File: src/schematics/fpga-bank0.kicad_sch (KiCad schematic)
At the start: 7 parts

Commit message: Updates the root page
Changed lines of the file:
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@@
+		)
+	)
+	(hierarchical_label "SRAM_A[0..12]"
+		(shape input)
+		(at 40.64 54.61 180)
+		(fields_autoplaced yes)
+		(effects
+			(font
+				(size 1.27 1.27)
+			)
+			(justify right)
 		)
 	)
@@
 		)
 	)
-	(hierarchical_label "{SDRAM}"
+	(hierarchical_label "SRAM_DQ[0..15]"
 		(shape input)
-		(at 95.25 59.69 180)
+		(at 73.66 116.84 0)
 		(fields_autoplaced yes)
 		(effects
@@
 				(size 1.27 1.27)
 			)
+			(justify left)
+		)
+	)
+	(hierarchical_label "SRAM_BA[0..1]"
+		(shape input)
+		(at 41.91 90.17 180)
+		(fields_autoplaced yes)
+		(effects
+			(font
+				(size 1.27 1.27)
+			)
 			(justify right)
+		)
+	)
+	(hierarchical_label "SRAM_~{WE}"
+		(shape input)
+		(at 54.61 124.46 0)
+		(fields_autoplaced yes)
+		(effects
+			(font
+				(size 1.27 1.27)
+			)
+			(justify left)
+		)
+	)
+	(hierarchical_label "SRAM_CLK"
+		(shape input)
+		(at 60.96 104.14 180)
+		(fields_autoplaced yes)
+		(effects
+			(font
+				(size 1.27 1.27)
+			)
+			(justify right)
+		)
+	)
+	(hierarchical_label "SRAM_~{CS}"
+		(shape input)
+		(at 60.96 109.22 180)
+		(fields_autoplaced yes)
+		(effects
+			(font
+				(size 1.27 1.27)
+			)
+			(justify right)
+		)
+	)
+	(hierarchical_label "SRAM_~{RAS}"
+		(shape input)
+		(at 54.61 119.38 0)
+		(fields_autoplaced yes)
+		(effects
+			(font
+				(size 1.27 1.27)
+			)
+			(justify left)
+		)
+	)
+	(hierarchical_label "SRAM_~{CAS}"
+		(shape input)
+		(at 54.61 121.92 0)
+		(fields_autoplaced yes)
+		(effects
+			(font
+				(size 1.27 1.27)
+			)
+			(justify left)
+		)
+	)
+	(hierarchical_label "SRAM_DQML"
+		(shape input)
+		(at 54.61 114.3 0)
+		(fields_autoplaced yes)
+		(effects
+			(font
+				(size 1.27 1.27)
+			)
+			(justify left)
+		)
+	)
+	(hierarchical_label "SRAM_CKE"
+		(shape input)
+		(at 60.96 106.68 180)
+		(fields_autoplaced yes)
+		(effects
+			(font
+				(size 1.27 1.27)
+			)
+			(justify right)
+		)
+	)
+	(hierarchical_label "SRAM_DQMH"
+		(shape input)
+		(at 54.61 116.84 0)
+		(fields_autoplaced yes)
+		(effects
+			(font
+				(size 1.27 1.27)
+			)
+			(justify left)
 		)
 	)
@@
 		(instances
 			(project "ecap5-bsom"
-				(path "/c5fd18a3-9aa0-4151-b6e0-94da3d606686/9ec64d27-698a-408d-bb9c-7e381193a80d/a27a4945-d3aa-4752-b726-05ef96a067ff"
+				(path "/c5fd18a3-9aa0-4151-b6e0-94da3d606686/6e8ffa03-3d0b-48ef-9cef-06edc52c2bd8"
 					(reference "C48")
 					(unit 1)
@@
 		(instances
 			(project "ecap5-bsom"
-				(path "/c5fd18a3-9aa0-4151-b6e0-94da3d606686/9ec64d27-698a-408d-bb9c-7e381193a80d/a27a4945-d3aa-4752-b726-05ef96a067ff"
+				(path "/c5fd18a3-9aa0-4151-b6e0-94da3d606686/6e8ffa03-3d0b-48ef-9cef-06edc52c2bd8"
 					(reference "#PWR026")
 					(unit 1)
@@
 		(instances
 			(project "ecap5-bsom"
-				(path "/c5fd18a3-9aa0-4151-b6e0-94da3d606686/9ec64d27-698a-408d-bb9c-7e381193a80d/a27a4945-d3aa-4752-b726-05ef96a067ff"
+				(path "/c5fd18a3-9aa0-4151-b6e0-94da3d606686/6e8ffa03-3d0b-48ef-9cef-06edc52c2bd8"
 					(reference "C51")
 					(unit 1)
@@
 		(instances
 			(project "ecap5-bsom"
-				(path "/c5fd18a3-9aa0-4151-b6e0-94da3d606686/9ec64d27-698a-408d-bb9c-7e381193a80d/a27a4945-d3aa-4752-b726-05ef96a067ff"
+				(path "/c5fd18a3-9aa0-4151-b6e0-94da3d606686/6e8ffa03-3d0b-48ef-9cef-06edc52c2bd8"
 					(reference "#PWR029")
 					(unit 1)
@@
 		(instances
 			(project "ecap5-bsom"
-				(path "/c5fd18a3-9aa0-4151-b6e0-94da3d606686/9ec64d27-698a-408d-bb9c-7e381193a80d/a27a4945-d3aa-4752-b726-05ef96a067ff"
+				(path "/c5fd18a3-9aa0-4151-b6e0-94da3d606686/6e8ffa03-3d0b-48ef-9cef-06edc52c2bd8"
 					(reference "#PWR025")
 					(unit 1)
@@
 		(instances
 			(project "ecap5-bsom"
-				(path "/c5fd18a3-9aa0-4151-b6e0-94da3d606686/9ec64d27-698a-408d-bb9c-7e381193a80d/a27a4945-d3aa-4752-b726-05ef96a067ff"
+				(path "/c5fd18a3-9aa0-4151-b6e0-94da3d606686/6e8ffa03-3d0b-48ef-9cef-06edc52c2bd8"
 					(reference "#PWR028")
 					(unit 1)
@@
 		(instances
 			(project "ecap5-bsom"
-				(path "/c5fd18a3-9aa0-4151-b6e0-94da3d606686/9ec64d27-698a-408d-bb9c-7e381193a80d/a27a4945-d3aa-4752-b726-05ef96a067ff"
+				(path "/c5fd18a3-9aa0-4151-b6e0-94da3d606686/6e8ffa03-3d0b-48ef-9cef-06edc52c2bd8"
 					(reference "C52")
 					(unit 1)
@@
 		(instances
 			(project "ecap5-bsom"
-				(path "/c5fd18a3-9aa0-4151-b6e0-94da3d606686/9ec64d27-698a-408d-bb9c-7e381193a80d/a27a4945-d3aa-4752-b726-05ef96a067ff"
+				(path "/c5fd18a3-9aa0-4151-b6e0-94da3d606686/6e8ffa03-3d0b-48ef-9cef-06edc52c2bd8"
 					(reference "U6")
 					(unit 2)
@@
 		(instances
 			(project "ecap5-bsom"
-				(path "/c5fd18a3-9aa0-4151-b6e0-94da3d606686/9ec64d27-698a-408d-bb9c-7e381193a80d/a27a4945-d3aa-4752-b726-05ef96a067ff"
+				(path "/c5fd18a3-9aa0-4151-b6e0-94da3d606686/6e8ffa03-3d0b-48ef-9cef-06edc52c2bd8"
 					(reference "C50")
 					(unit 1)
@@
 		(instances
 			(project "ecap5-bsom"
-				(path "/c5fd18a3-9aa0-4151-b6e0-94da3d606686/9ec64d27-698a-408d-bb9c-7e381193a80d/a27a4945-d3aa-4752-b726-05ef96a067ff"
+				(path "/c5fd18a3-9aa0-4151-b6e0-94da3d606686/6e8ffa03-3d0b-48ef-9cef-06edc52c2bd8"
 					(reference "#PWR030")
 					(unit 1)
@@
 		(instances
 			(project "ecap5-bsom"
-				(path "/c5fd18a3-9aa0-4151-b6e0-94da3d606686/9ec64d27-698a-408d-bb9c-7e381193a80d/a27a4945-d3aa-4752-b726-05ef96a067ff"
+				(path "/c5fd18a3-9aa0-4151-b6e0-94da3d606686/6e8ffa03-3d0b-48ef-9cef-06edc52c2bd8"
 					(reference "#PWR031")
 					(unit 1)
@@
 		(instances
 			(project "ecap5-bsom"
-				(path "/c5fd18a3-9aa0-4151-b6e0-94da3d606686/9ec64d27-698a-408d-bb9c-7e381193a80d/a27a4945-d3aa-4752-b726-05ef96a067ff"
+				(path "/c5fd18a3-9aa0-4151-b6e0-94da3d606686/6e8ffa03-3d0b-48ef-9cef-06edc52c2bd8"
 					(reference "C53")
 					(unit 1)
@@
 		(instances
 			(project "ecap5-bsom"
-				(path "/c5fd18a3-9aa0-4151-b6e0-94da3d606686/9ec64d27-698a-408d-bb9c-7e381193a80d/a27a4945-d3aa-4752-b726-05ef96a067ff"
+				(path "/c5fd18a3-9aa0-4151-b6e0-94da3d606686/6e8ffa03-3d0b-48ef-9cef-06edc52c2bd8"
 					(reference "C49")
 					(unit 1)
@@
 		(instances
 			(project "ecap5-bsom"
-				(path "/c5fd18a3-9aa0-4151-b6e0-94da3d606686/9ec64d27-698a-408d-bb9c-7e381193a80d/a27a4945-d3aa-4752-b726-05ef96a067ff"
+				(path "/c5fd18a3-9aa0-4151-b6e0-94da3d606686/6e8ffa03-3d0b-48ef-9cef-06edc52c2bd8"
 					(reference "#PWR027")
 					(unit 1)

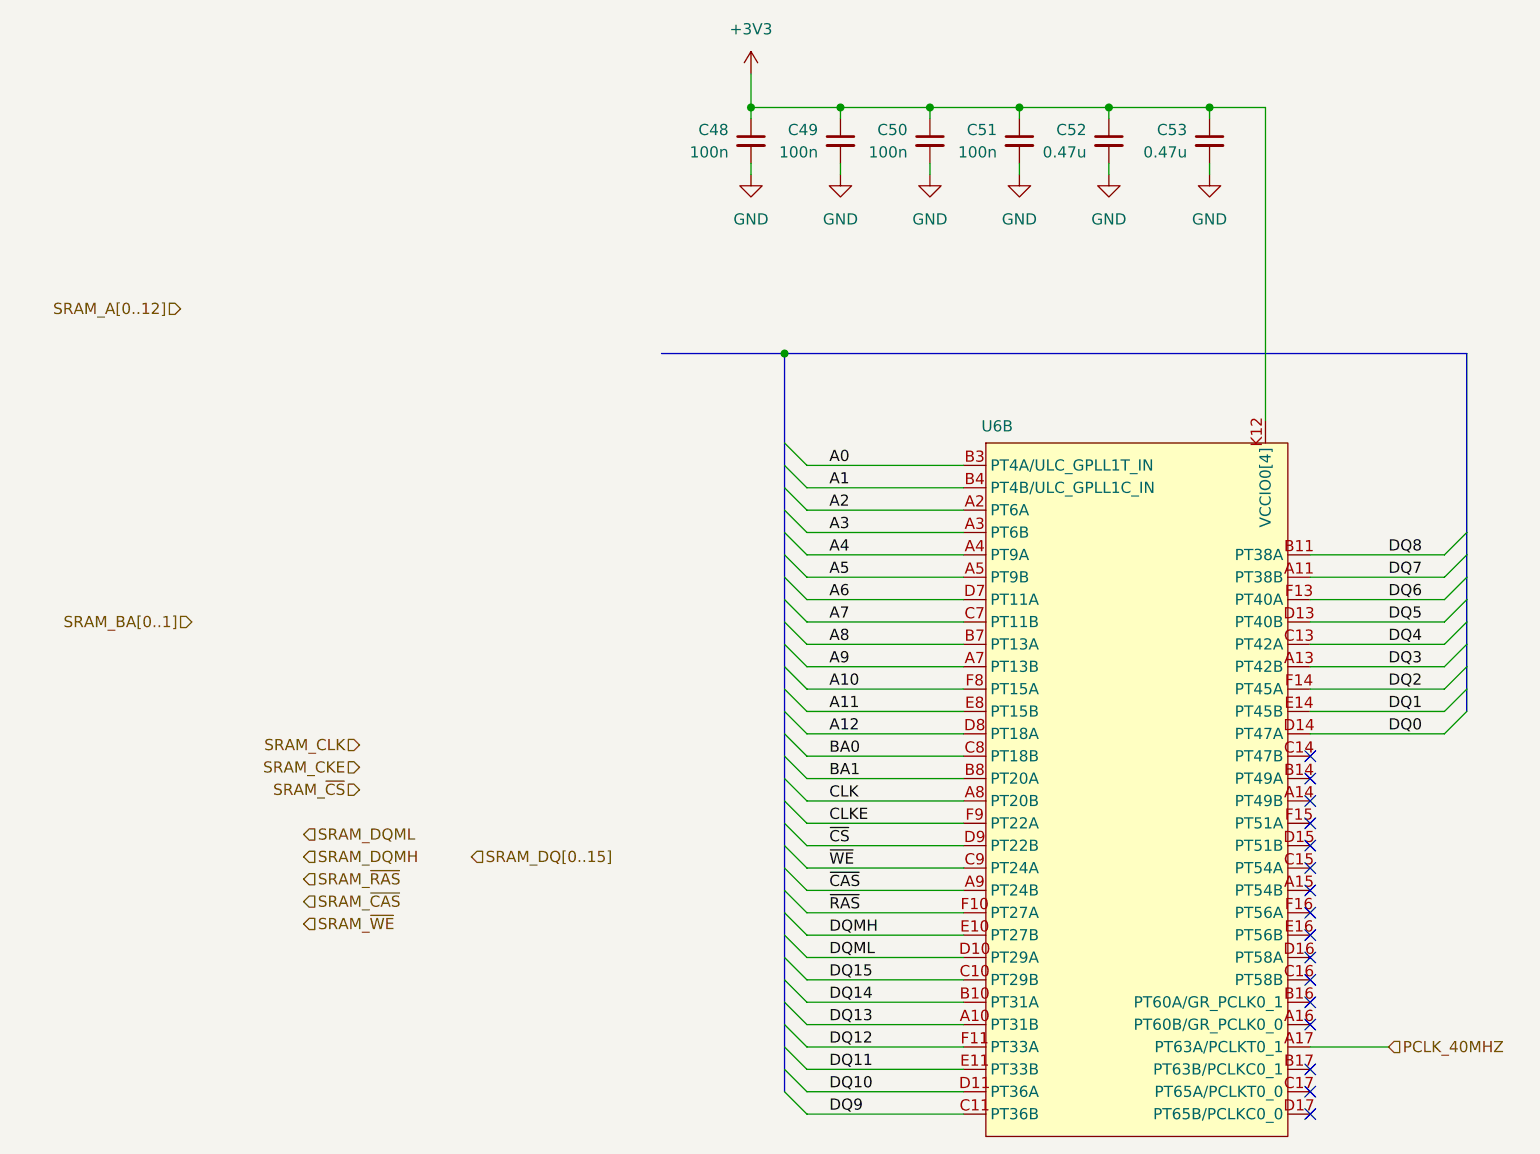
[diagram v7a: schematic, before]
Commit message: Adds a revision history table
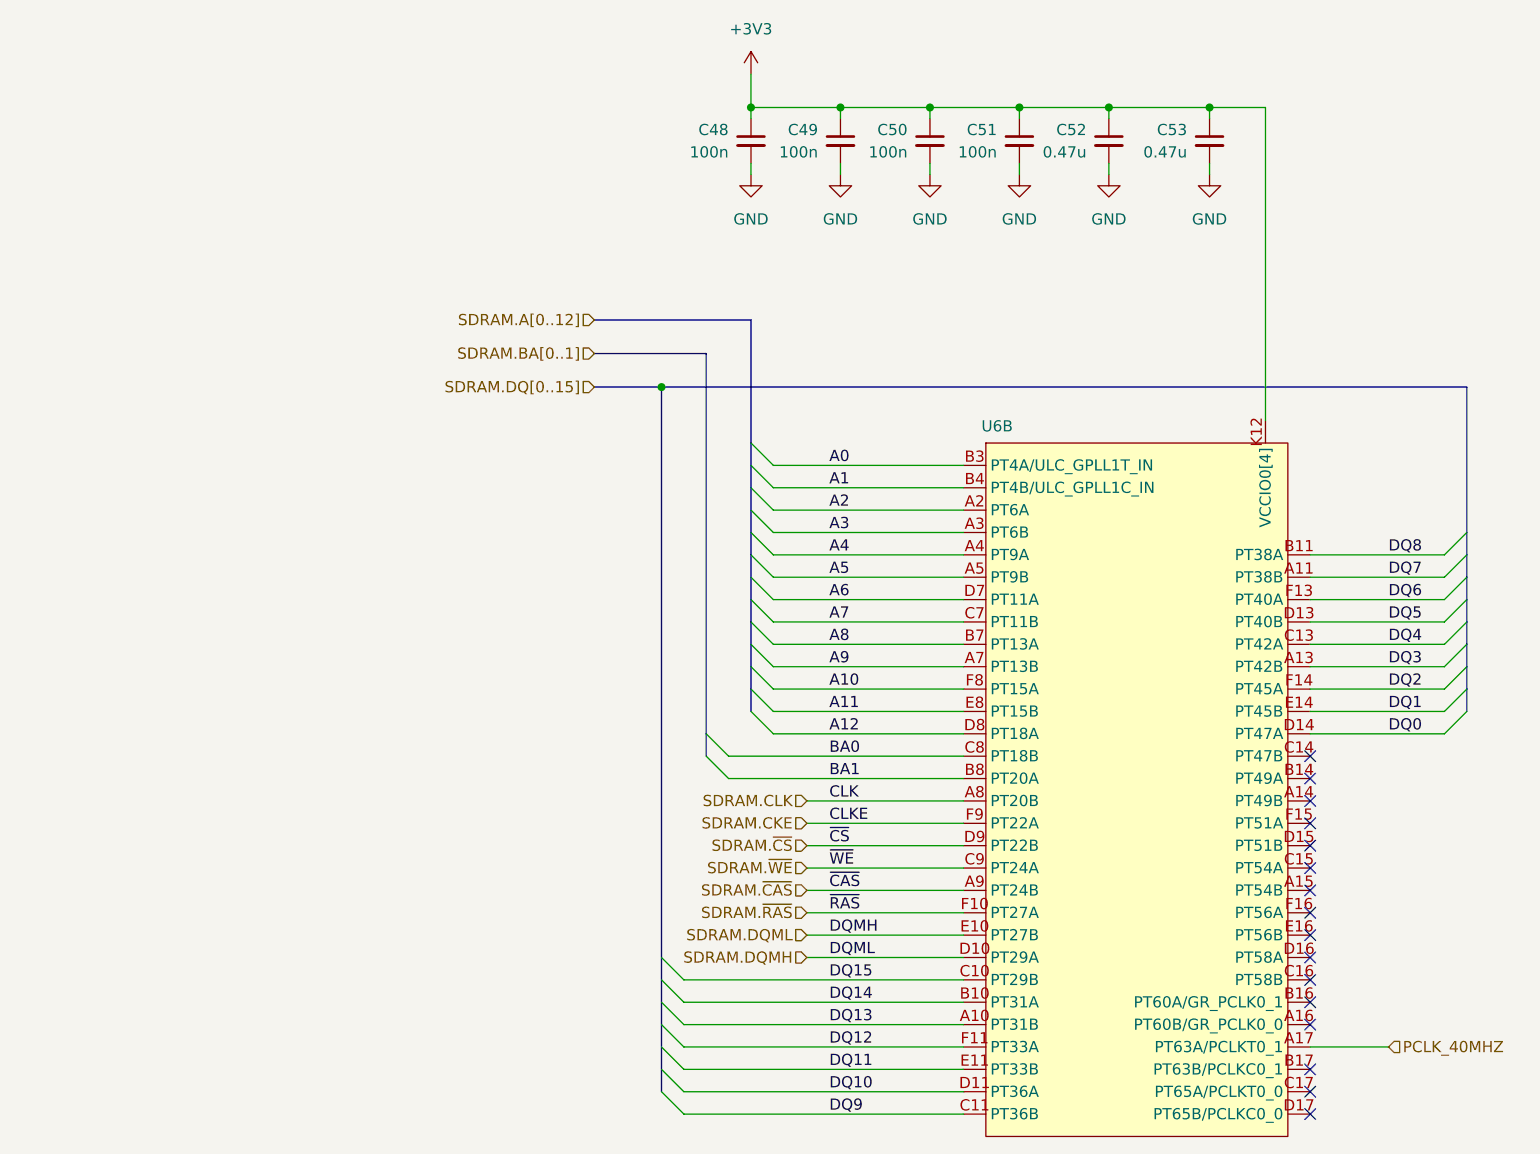
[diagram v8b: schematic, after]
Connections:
- net CLK renamed SDRAM.CLK
- net CLKE renamed SDRAM.CKE
- net DQMH renamed SDRAM.DQML
- net DQML renamed SDRAM.DQMH
- net ~{CAS} renamed SDRAM.~{CAS}
- net ~{CS} renamed SDRAM.~{CS}
- net ~{RAS} renamed SDRAM.~{RAS}
- net ~{WE} renamed SDRAM.~{WE}
